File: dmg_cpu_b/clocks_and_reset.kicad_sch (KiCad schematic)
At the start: 112 parts

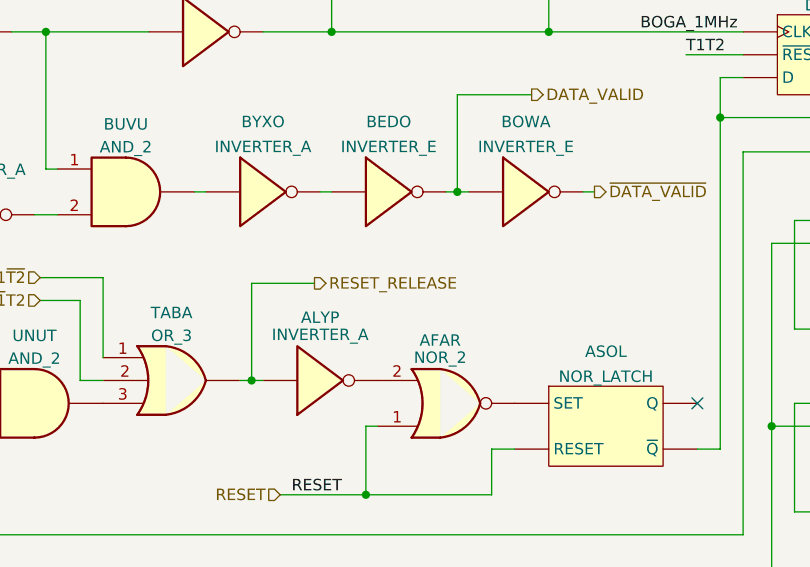
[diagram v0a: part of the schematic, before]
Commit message: Sprite Y comparator changes made from review.
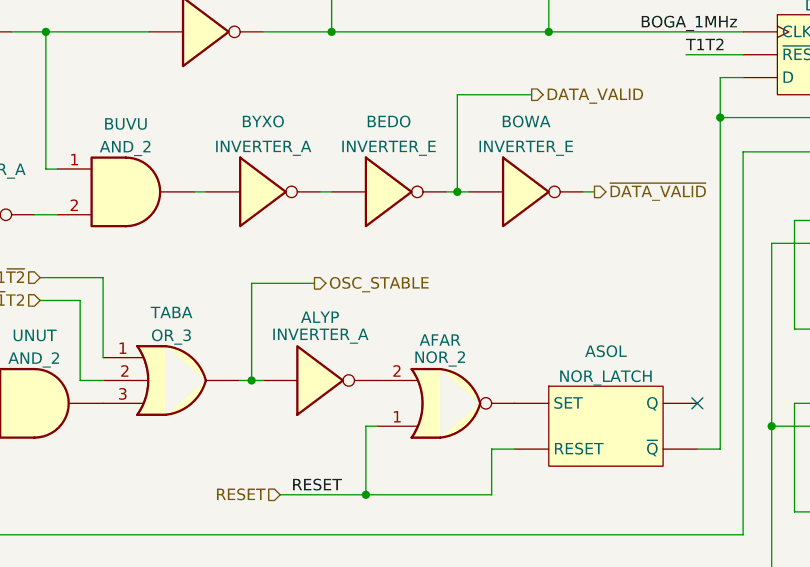
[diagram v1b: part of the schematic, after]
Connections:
- net RESET_RELEASE renamed OSC_STABLE
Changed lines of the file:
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@@
     (effects (font (size 1.27 1.27)) (justify left))
   )
-  (hierarchical_label "RESET_RELEASE" (shape output) (at 253.365 62.865 0)
+  (hierarchical_label "OSC_STABLE" (shape output) (at 253.365 62.865 0)
     (effects (font (size 1.27 1.27)) (justify left))
   )

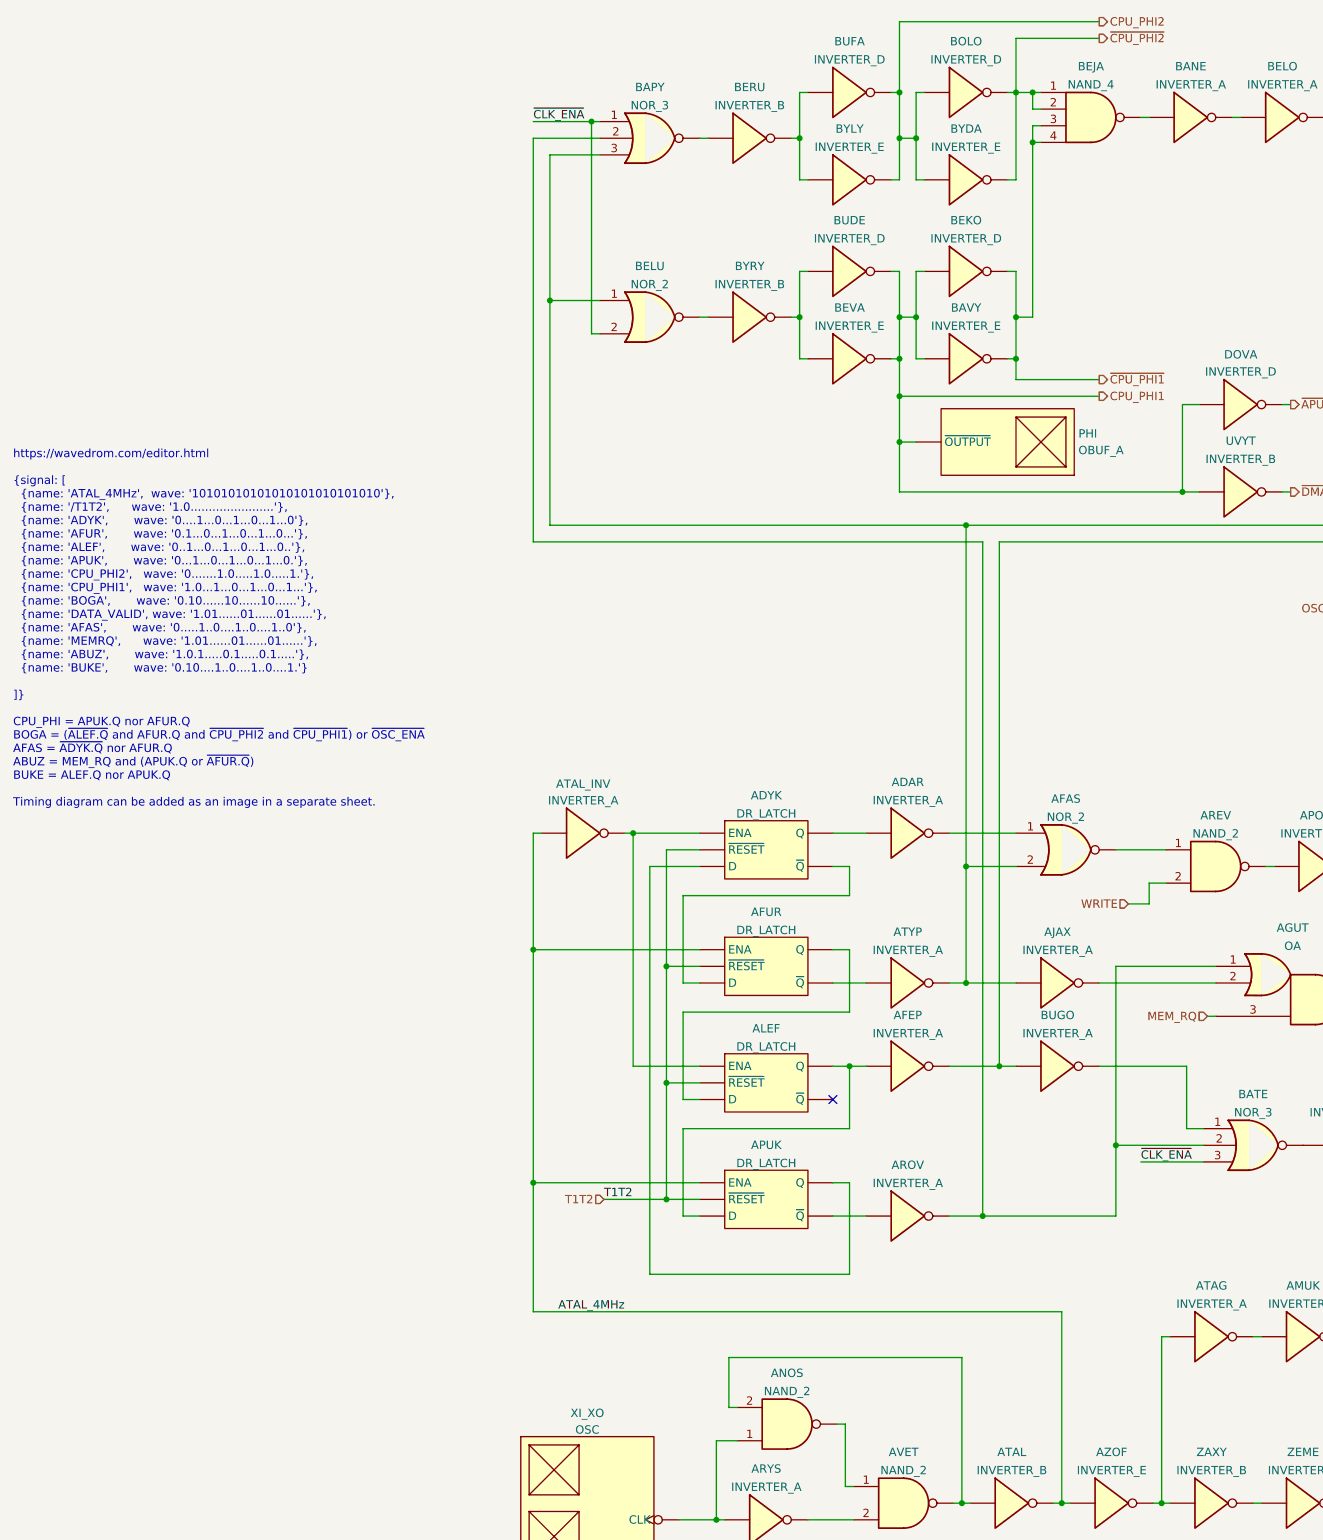
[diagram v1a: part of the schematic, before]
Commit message: Issues addressed. Renaming and inverted signal names to make thing more consistent and meaningful.
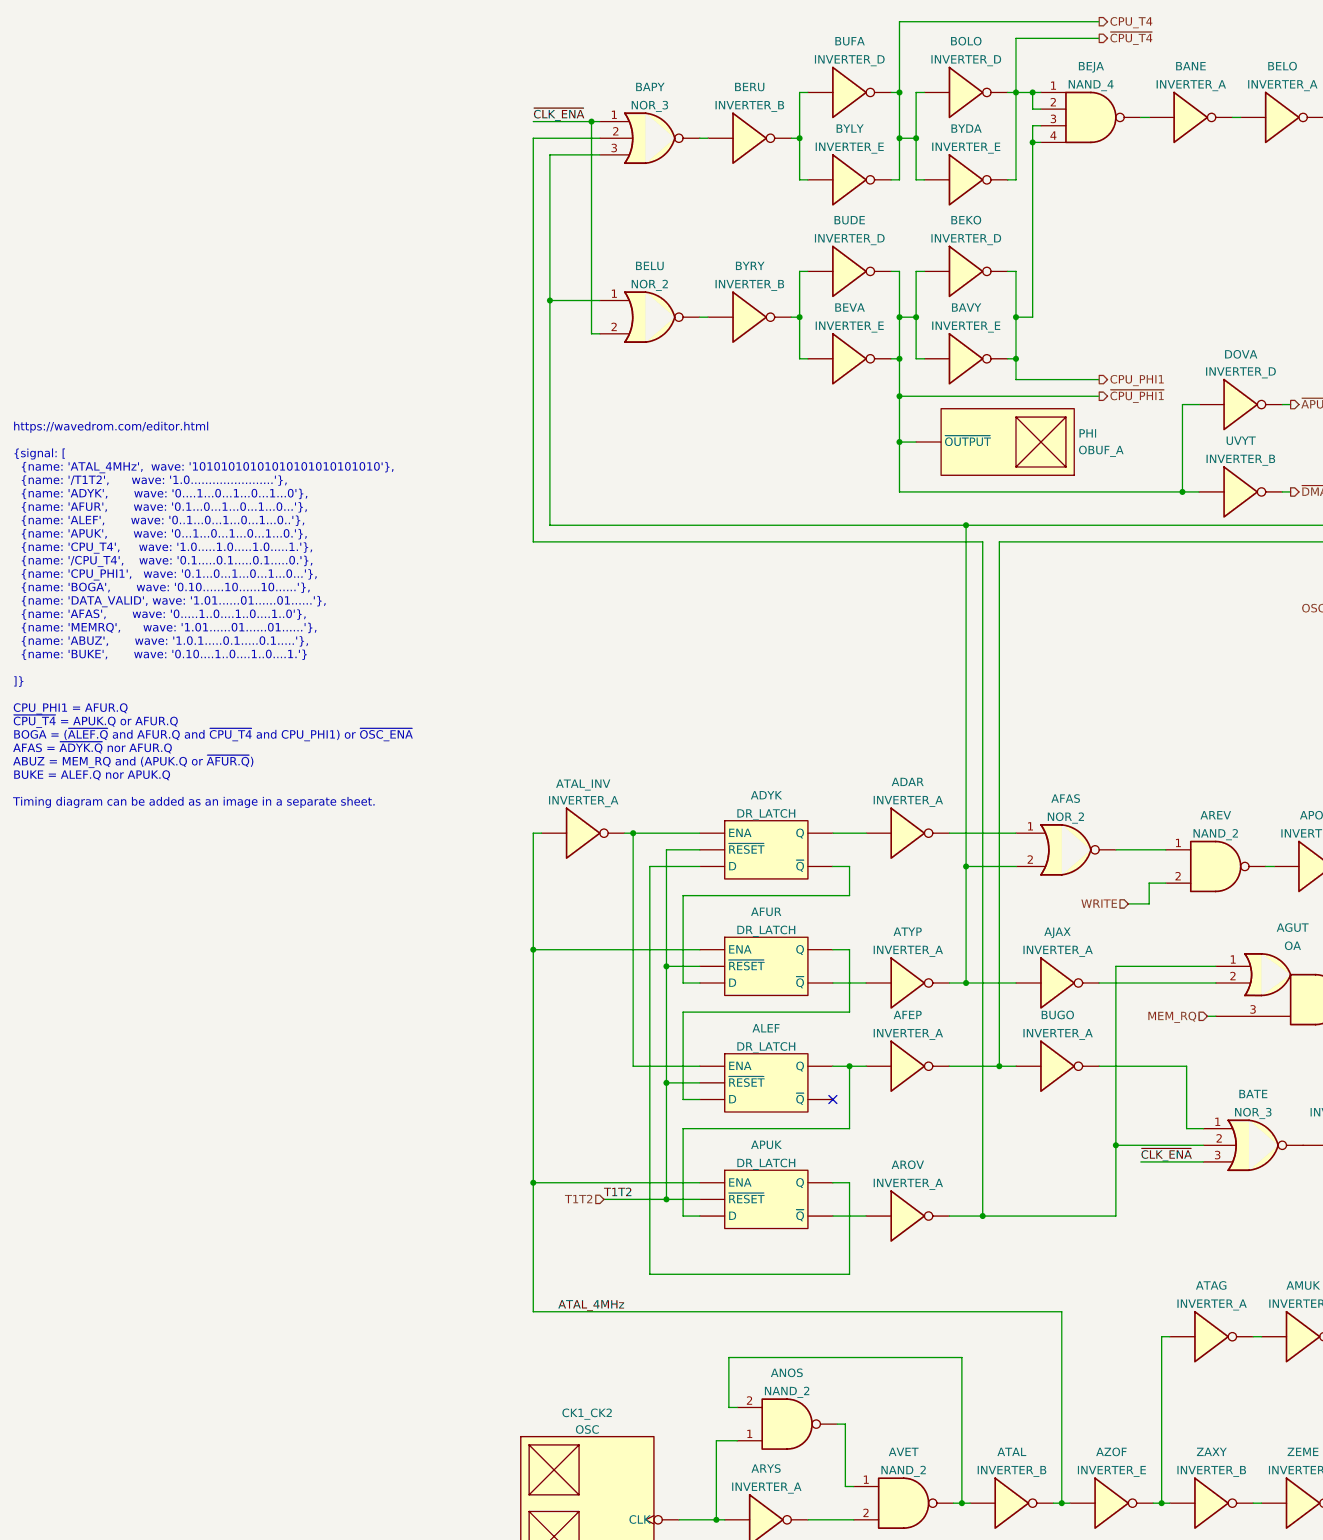
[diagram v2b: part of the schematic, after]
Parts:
- renumbered XI_XO to CK1_CK2
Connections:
- net CPU_PHI1: now also BAVY.2, BEJA.3, BEJA.4, BEKO.2; no longer BAVY.1, BEKO.1, BEVA.2, BUDE.2, DOVA.1, PHI.1 (~{OUTPUT}), UVYT.1
- net ~{CPU_PHI1}: now also BAVY.1, BEKO.1, BEVA.2, BUDE.2, DOVA.1, PHI.1 (~{OUTPUT}), UVYT.1; no longer BAVY.2, BEJA.3, BEJA.4, BEKO.2
- net CPU_PHI2 renamed CPU_T4
- net ~{CPU_PHI2} renamed ~{CPU_T4}
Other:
- note added: "https://wavedrom.com/editor.html {signal: [ {name: 'ATAL_4MHz', wave: '10101010101010101010101010'}, {name: '/T1T2', wave: '1.0.......................'}, {name: 'ADYK', wave: '0....1...0...1...0...1...0'}, {name: 'AFUR', wave: '0.1...0...1...0...1...0...'}, {name: 'ALEF', wave: '0..1...0...1...0...1...0..'}, {name: 'APUK', wave: '0...1...0...1...0...1...0.'}, {name: 'CPU_T4', wave: '1.0.....1.0..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"
- note removed: "https://wavedrom.com/editor.html {signal: [ {name: 'ATAL_4MHz', wave: '10101010101010101010101010'}, {name: '/T1T2', wave: '1.0.......................'}, {name: 'ADYK', wave: '0....1...0...1...0...1...0'}, {name: 'AFUR', wave: '0.1...0...1...0...1...0...'}, {name: 'ALEF', wave: '0..1...0...1...0...1...0..'}, {name: 'APUK', wave: '0...1...0...1...0...1...0.'}, {name: 'CPU_PHI2', wave: '0.......1.0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"
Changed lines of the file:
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@@
     (effects (font (size 1.27 1.27)) (justify left bottom))
   )
-  (text "https://wavedrom.com/editor.html\n\n{signal: [\n  {name: 'ATAL_4MHz',  wave: '10101010101010101010101010'},\n  {name: '/T1T2',      wave: '1.0.......................'},\n  {name: 'ADYK',       wave: '0....1...0...1...0...1...0'},\n  {name: 'AFUR',       wave: '0.1...0...1...0...1...0...'},\n  {name: 'ALEF',       wave: '0..1...0...1...0...1...0..'},\n  {name: 'APUK',       wave: '0...1...0...1...0...1...0.'},\n  {name: 'CPU_PHI2',   wave: '0.......1.0.....1.0.....1.'},\n  {name: 'CPU_PHI1',   wave: '1.0...1...0...1...0...1...'},\n  {name: 'BOGA',       wave: '0.10......10......10......'},\n  {name: 'DATA_VALID', wave: '1.01......01......01......'},\n  {name: 'AFAS',       wave: '0.....1..0....1..0....1..0'},\n  {name: 'MEMRQ',      wave: '1.01......01......01......'},\n  {name: 'ABUZ',       wave: '1.0.1.....0.1.....0.1.....'},\n  {name: 'BUKE',       wave: '0.10....1..0....1..0....1.'}\n  \n]}\n\nCPU_PHI = APUK.Q nor AFUR.Q\nBOGA = (~{ALEF.Q} and AFUR.Q and ~{CPU_PHI2} and ~{CPU_PHI1}) or ~{OSC_ENA} \nAFAS = ~{ADYK.Q} nor AFUR.Q \nABUZ = MEM_RQ and (APUK.Q or ~{AFUR.Q})\nBUKE = ALEF.Q nor APUK.Q\n\nTiming diagram can be added as an image in a separate sheet."
+  (text "https://wavedrom.com/editor.html\n\n{signal: [\n  {name: 'ATAL_4MHz',  wave: '10101010101010101010101010'},\n  {name: '/T1T2',      wave: '1.0.......................'},\n  {name: 'ADYK',       wave: '0....1...0...1...0...1...0'},\n  {name: 'AFUR',       wave: '0.1...0...1...0...1...0...'},\n  {name: 'ALEF',       wave: '0..1...0...1...0...1...0..'},\n  {name: 'APUK',       wave: '0...1...0...1...0...1...0.'},\n  {name: 'CPU_T4',     wave: '1.0.....1.0.....1.0.....1.'},\n  {name: '/CPU_T4',    wave: '0.1.....0.1.....0.1.....0.'},\n  {name: 'CPU_PHI1',   wave: '0.1...0...1...0...1...0...'},\n  {name: 'BOGA',       wave: '0.10......10......10......'},\n  {name: 'DATA_VALID', wave: '1.01......01......01......'},\n  {name: 'AFAS',       wave: '0.....1..0....1..0....1..0'},\n  {name: 'MEMRQ',      wave: '1.01......01......01......'},\n  {name: 'ABUZ',       wave: '1.0.1.....0.1.....0.1.....'},\n  {name: 'BUKE',       wave: '0.10....1..0....1..0....1.'}\n  \n]}\n\nCPU_PHI1 = AFUR.Q\n~{CPU_T4} = APUK.Q or AFUR.Q\nBOGA = (~{ALEF.Q} and AFUR.Q and ~{CPU_T4} and CPU_PHI1) or ~{OSC_ENA} \nAFAS = ~{ADYK.Q} nor AFUR.Q \nABUZ = MEM_RQ and (APUK.Q or ~{AFUR.Q})\nBUKE = ALEF.Q nor APUK.Q\n\nTiming diagram can be added as an image in a separate sheet."
     (at -62.23 135.255 0)
     (effects (font (size 1.27 1.27)) (justify left bottom))
@@
     (effects (font (size 1.27 1.27)) (justify left))
   )
-  (hierarchical_label "~{CPU_PHI1}" (shape output) (at 103.505 69.85 0)
-    (effects (font (size 1.27 1.27)) (justify left))
-  )
-  (hierarchical_label "CPU_PHI2" (shape output) (at 103.505 15.24 0)
+  (hierarchical_label "CPU_PHI1" (shape output) (at 103.505 69.85 0)
+    (effects (font (size 1.27 1.27)) (justify left))
+  )
+  (hierarchical_label "CPU_T4" (shape output) (at 103.505 15.24 0)
     (effects (font (size 1.27 1.27)) (justify left))
   )
@@
     (effects (font (size 1.27 1.27)) (justify left))
   )
-  (hierarchical_label "~{CPU_PHI2}" (shape output) (at 103.505 17.78 0)
+  (hierarchical_label "~{CPU_T4}" (shape output) (at 103.505 17.78 0)
     (effects (font (size 1.27 1.27)) (justify left))
   )
@@
     (effects (font (size 1.27 1.27)) (justify right))
   )
-  (hierarchical_label "CPU_PHI1" (shape output) (at 103.505 72.39 0)
+  (hierarchical_label "~{CPU_PHI1}" (shape output) (at 103.505 72.39 0)
     (effects (font (size 1.27 1.27)) (justify left))
   )
@@
   (symbol (lib_id "DMG_CPU_Cells:OSC") (at 25.4 241.3 0) (unit 1)
     (in_bom yes) (on_board yes) (fields_autoplaced)
-    (property "Reference" "XI_XO" (id 0) (at 25.4 227.5672 0))
+    (property "Reference" "CK1_CK2" (id 0) (at 25.4 227.5672 0))
     (property "Value" "OSC" (id 1) (at 25.4 230.1041 0))
     (property "Footprint" "" (id 2) (at 25.4 246.38 0)

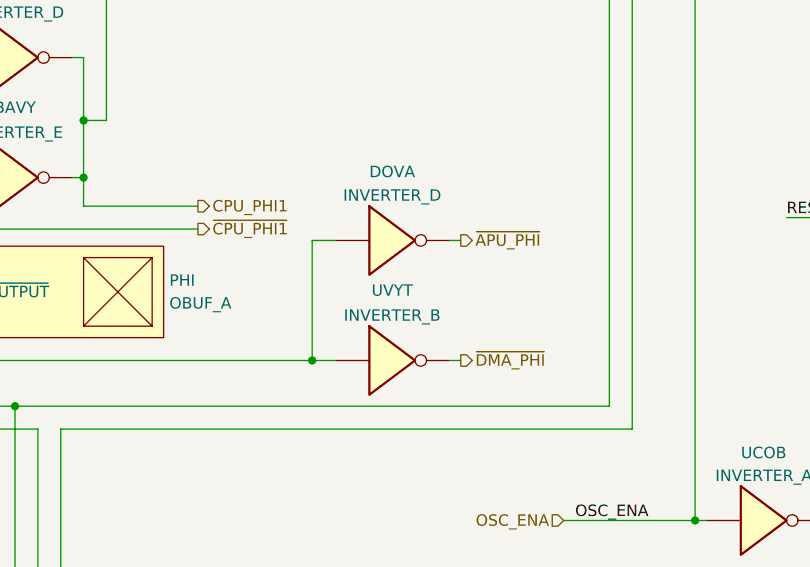
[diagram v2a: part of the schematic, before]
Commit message: Fixed PHI signals.
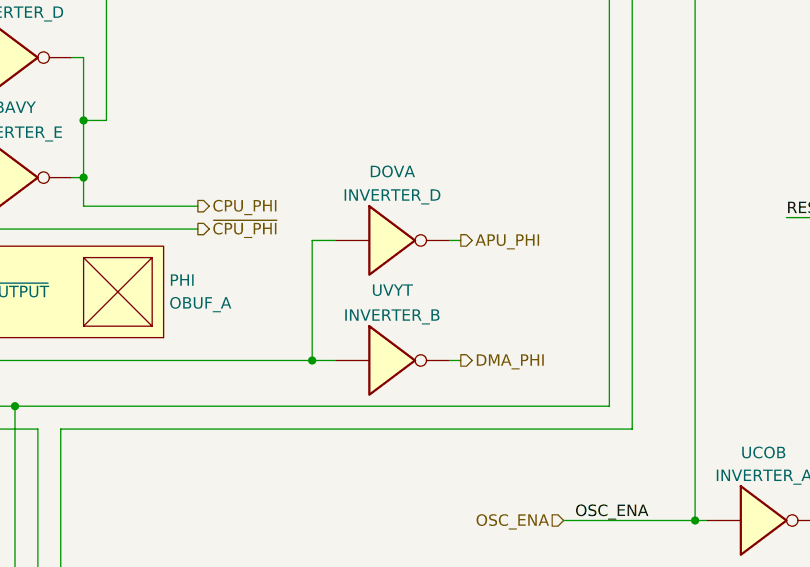
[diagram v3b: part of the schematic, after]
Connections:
- net CPU_PHI1 renamed CPU_PHI
- net ~{APU_PHI} renamed APU_PHI
- net ~{CPU_PHI1} renamed ~{CPU_PHI}
- net ~{DMA_PHI} renamed DMA_PHI
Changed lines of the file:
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@@
     (effects (font (size 1.27 1.27)) (justify left))
   )
-  (hierarchical_label "CPU_PHI1" (shape output) (at 103.505 69.85 0)
+  (hierarchical_label "CPU_PHI" (shape output) (at 103.505 69.85 0)
     (effects (font (size 1.27 1.27)) (justify left))
   )
@@
     (effects (font (size 1.27 1.27)) (justify right))
   )
-  (hierarchical_label "~{CPU_PHI1}" (shape output) (at 103.505 72.39 0)
+  (hierarchical_label "~{CPU_PHI}" (shape output) (at 103.505 72.39 0)
     (effects (font (size 1.27 1.27)) (justify left))
   )
@@
     (effects (font (size 1.27 1.27)) (justify right))
   )
-  (hierarchical_label "~{DMA_PHI}" (shape output) (at 132.715 86.995 0)
+  (hierarchical_label "DMA_PHI" (shape output) (at 132.715 86.995 0)
     (effects (font (size 1.27 1.27)) (justify left))
   )
@@
     (effects (font (size 1.27 1.27)) (justify right))
   )
-  (hierarchical_label "~{APU_PHI}" (shape output) (at 132.715 73.66 0)
+  (hierarchical_label "APU_PHI" (shape output) (at 132.715 73.66 0)
     (effects (font (size 1.27 1.27)) (justify left))
   )
